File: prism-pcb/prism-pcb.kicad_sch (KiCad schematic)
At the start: 0 parts

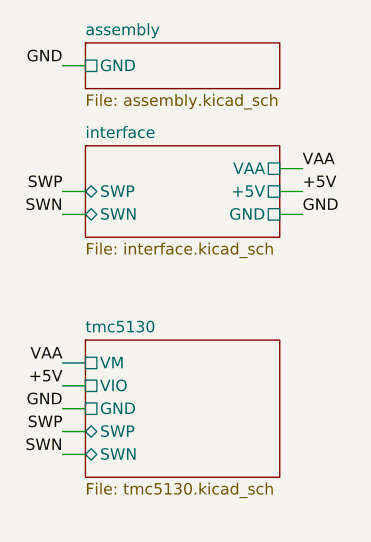
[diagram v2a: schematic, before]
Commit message: Update schematic to use external 5V supply
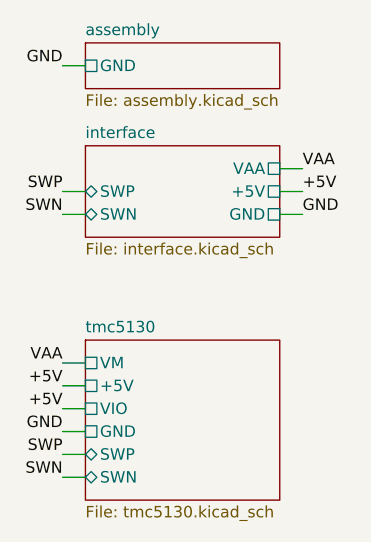
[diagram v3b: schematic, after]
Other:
- sheet tmc5130 ports: added +5V; removed none
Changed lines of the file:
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@@
   (title_block
     (title "prism-pcb")
-    (date "2024-07-25")
-    (rev "1.1")
+    (date "2024-08-07")
+    (rev "1.2")
     (company "Howard Hughes Medical Institute")
   )
@@
     (stroke (width 0) (type default))
   )
-  (wire (pts (xy 130.81 96.52) (xy 128.27 96.52))
+  (wire (pts (xy 130.81 99.06) (xy 128.27 99.06))
     (stroke (width 0) (type default))
   )
@@
     (stroke (width 0) (type default))
   )
-  (wire (pts (xy 128.27 93.98) (xy 130.81 93.98))
+  (wire (pts (xy 128.27 96.52) (xy 130.81 96.52))
     (stroke (width 0) (type default))
   )
@@
     (stroke (width 0) (type default))
   )
-  (wire (pts (xy 130.81 99.06) (xy 128.27 99.06))
+  (wire (pts (xy 130.81 101.6) (xy 128.27 101.6))
     (stroke (width 0) (type default))
   )
   (wire (pts (xy 154.94 69.85) (xy 152.4 69.85))
+    (stroke (width 0) (type default))
+  )
+  (wire (pts (xy 128.27 93.98) (xy 130.81 93.98))
     (stroke (width 0) (type default))
   )
@@
     (effects (font (size 1.27 1.27)) (justify left bottom))
   )
-  (label "SWN" (at 128.27 99.06 180) (fields_autoplaced)
+  (label "SWN" (at 128.27 101.6 180) (fields_autoplaced)
     (effects (font (size 1.27 1.27)) (justify right bottom))
   )
   (label "+5V" (at 128.27 91.44 180) (fields_autoplaced)
+    (effects (font (size 1.27 1.27)) (justify right bottom))
+  )
+  (label "+5V" (at 128.27 93.98 180) (fields_autoplaced)
     (effects (font (size 1.27 1.27)) (justify right bottom))
   )
@@
     (effects (font (size 1.27 1.27)) (justify right bottom))
   )
-  (label "GND" (at 128.27 93.98 180) (fields_autoplaced)
+  (label "GND" (at 128.27 96.52 180) (fields_autoplaced)
     (effects (font (size 1.27 1.27)) (justify right bottom))
   )
@@
     (effects (font (size 1.27 1.27)) (justify right bottom))
   )
-  (label "SWP" (at 128.27 96.52 180) (fields_autoplaced)
+  (label "SWP" (at 128.27 99.06 180) (fields_autoplaced)
     (effects (font (size 1.27 1.27)) (justify right bottom))
   )
@@
     (effects (font (size 1.27 1.27)) (justify left bottom))
   )
-  (sheet (at 130.81 86.36) (size 21.59 15.24) (fields_autoplaced)
+  (sheet (at 130.81 86.36) (size 21.59 17.78) (fields_autoplaced)
     (stroke (width 0.1524) (type solid))
     (fill (color 0 0 0 0.0000))
@@
       (effects (font (size 1.27 1.27)) (justify left bottom))
     )
-    (property "Sheetfile" "tmc5130.kicad_sch" (at 130.81 102.1846 0)
+    (property "Sheetfile" "tmc5130.kicad_sch" (at 130.81 104.7246 0)
       (effects (font (size 1.27 1.27)) (justify left top))
     )
@@
       (effects (font (size 1.27 1.27)) (justify left))
     )
-    (pin "VIO" passive (at 130.81 91.44 180)
+    (pin "VIO" passive (at 130.81 93.98 180)
       (effects (font (size 1.27 1.27)) (justify left))
     )
-    (pin "GND" passive (at 130.81 93.98 180)
+    (pin "GND" passive (at 130.81 96.52 180)
       (effects (font (size 1.27 1.27)) (justify left))
     )
-    (pin "SWN" bidirectional (at 130.81 99.06 180)
+    (pin "SWN" bidirectional (at 130.81 101.6 180)
       (effects (font (size 1.27 1.27)) (justify left))
     )
-    (pin "SWP" bidirectional (at 130.81 96.52 180)
+    (pin "SWP" bidirectional (at 130.81 99.06 180)
       (effects (font (size 1.27 1.27)) (justify left))
     )
+    (pin "+5V" passive (at 130.81 91.44 180)
+      (effects (font (size 1.27 1.27)) (justify left))
+    )
